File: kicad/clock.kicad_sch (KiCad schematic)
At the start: 182 parts, among them J1 USB4160-03-0230-C, J10 Knob: EM14 enc+SW (top face), J11 Radio-off toggle (rear), J12 NeoPixel ext (5V/DATA/GND, po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, J2 PROG, J3 Speaker DMA58-4 (4R), J6 DM3AT-SF-PEJM5, J7 Sensor board (BME688+TSL2591+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, J9 Wake COB 12V (warm+cool), M1 X40.879, Q1 2N7002, Q2 AO3401A, Q3 2N7002, Q4 AO3401A, Q6 AO3400A, Q7 AO3400A, Q8 2N7002, Q9 AO3401A, SW1 RESET, SW2 BOOT, U1 CH224K, U10 LTC4412ES6, U11 TB6612FNG, U12 TB6612FNG, U13 MCP23017, U14 QRE1113GR, U15 SN74AHCT1G125, U16 USBLC6-2SC6, U2 LT3652EMSE, U3 HY2111-GB, U4 AOSD32334C, U5 TPS61023, U6 TLV62569DBVR, U7 TPS55340PWPR, U8 ESP32-S3-WROOM-1-N16R8, U9 TAS5760MDAPR, Y1 32.768kHz

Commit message: review phase 0+1: fix the three blocking schematic defects
Adds kicad/REVEIW.md (full design review of clock.kicad_sch/.kicad_pcb at
7ec2534) and fixes the three findings that stop the board working:

#1 Q4 (LTC4412 PVDD mux) had drain on PVDD and source on +5V, so its body
   diode dumped the 12 V rail into +5V the moment BOOST12_EN went high --
   past abs-max for U5 (7 V), U6 (6 V), U15 (7 V), the SK6812s and the EM14.
   Now drain->+5V, source->PVDD per the LTC4412 datasheet.

#2 TAS5760M PBTL tied OUTA+||OUTB+ and OUTA-||OUTB-, shorting two anti-phase
   half-bridges (hard PVDD->PGND every switching cycle). TI SLOS772F fig.64/65
   pair A+||A- and B+||B-; bootstraps follow their own leg (C181/C182 swap
   roles, positions unchanged).

#3 LT3652 C_TIMER was 100 nF = 26 min EOC and a 3.3 min precondition window,
   which latches a flat cell off as a bad battery. 1 uF -> 4.4 h / 33 min,
   same 0603 land and an existing BOM line.

Supporting changes:
- pcb_build.py: refuse to run without PCB_BUILD_WIPE_ROUTING=1. It builds with
  CreateEmptyBoard() and would destroy the 1884 routed segments / 555 vias /
  4 filled zones the board has carried since 91c5087.
- sch2.py: _xf() mirrored before rotating, KiCad mirrors after -- silently
  swaps the mirror axes at rot 90/270. Latent until Q4 needed a mirror.
- parts_db.py: fold M1's hand-written "DO NOT MOUNT" assembly note into the
  Notes field, so stamp_bom.py stops wiping it on every run.
- review_check.py: standing assertions for the review findings.

ERC 0. Netlist diff vs the pre-fix schematic is exactly the 6 intended node
moves. PCB routing untouched -- the F8 sync and re-route are still to do.

Co-Authored-By: Claude Opus 5 <noreply@anthropic.com>
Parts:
- C104: value 100nF -> 1uF; MPN CL10B104KB8NNNC -> CL10B105KA8NNNC
- M1: Notes Custom footprint; shafts pass through the board. Long lead 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 -> DO NOT MOUNT. Customer will mount part after PCB reception.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
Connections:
- net +5V: now also Q4.3 (D); no longer Q4.2 (S)
- net PVDD: now also Q4.2 (S); no longer Q4.3 (D)
- net at C181.2, C183.2, L6.1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: now also U9.20 (SPK_OUTB+); no longer U9.26 (SPK_OUTA-)
- net at C182.1: now also U9.25 (BSTRPA-); no longer U9.19 (BSTRPB+)
- net at C180.2, C182.2, L5.1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: now also U9.26 (SPK_OUTA-); no longer U9.20 (SPK_OUTB+)
- net at C181.1: now also U9.19 (BSTRPB+); no longer U9.25 (BSTRPA-)
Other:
- company: Tibo Mauron -> (none)
- title: Wooden Clock - main board -> Wooden Smart Clock — main board
- moved on the sheet: Q4

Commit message: review phase 1b: cheap schematic follow-ons (#11 #12 #15 #17)
#11 J7 pin 6 was NC here but the sensor board drives ALS_INT (TSL2591 INT)
    onto it, so the light sensor could only be polled. Landed on the
    expander's free GPB3.
#12 J7 value string said LIS3DH; the sensor board carries a BNO085.
#15 With VBAT_DIV_EN low, Q3 opens the bottom of the divider and R22 pulls
    the ADC node to V_cell (~4.05 V) -- above the ESP32's VDD+0.3 abs-max, so
    IO1 sits forward-biasing its own upper ESD diode. D14 (same BAT42W/SOD-123
    as D13, no new BOM line) clamps it to ~3.5 V.
#17 Encoder A/B divider 100k/200k -> 10k/20k: same 1:2 ratio and the same
    worst-case 3.5 V at the pin, but 6.7k instead of 66.7k driving a ~40 mm
    run past both stepper drivers and the class-D amp. Costs 2x167 uA.

#13 (R1 dissipating 137 mW in a 100 mW 0603) is deliberately NOT in this
batch: it needs a 1206 land or a high-power 0603 part, i.e. an MPN sourced
and verified, and a _REF override since parts_db keys resistors by value only.

ERC 0. Netlist diff vs 1f3736a is exactly: +ALS_INT (J7.6+U13.4), D14 onto
+3V3/VBAT_SENSE, the two unconnected- pseudo-nets gone, and 5 value changes.
PCB still untouched -- D14 needs placing, and the Phase 2 re-route is next.

Co-Authored-By: Claude Opus 5 <noreply@anthropic.com>
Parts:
- added D14: BAT42W, Diode_SMD:D_SOD-123, symbol Device:D_Schottky
- J7: value Sensor board (BME688+TSL2591+LIS3DH) -> Sensor board (BME688+TSL2591+BNO085)
- R111, R112: value 100k -> 10k; MPN RC0603FR-07100KL -> RC0603FR-0710KL
- R114, R115: value 200k -> 20k; MPN RC0603FR-07200KL -> RC0603FR-0720KL
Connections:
- net +3V3: now also D14.1 (K)
- net VBAT_SENSE: now also D14.2 (A)
- net ALS_INT: now reaches J7.6 (Pin_6)
- net ALS_INT: now also U13.4 (GPB3)
- no-connect marks 20 -> 18

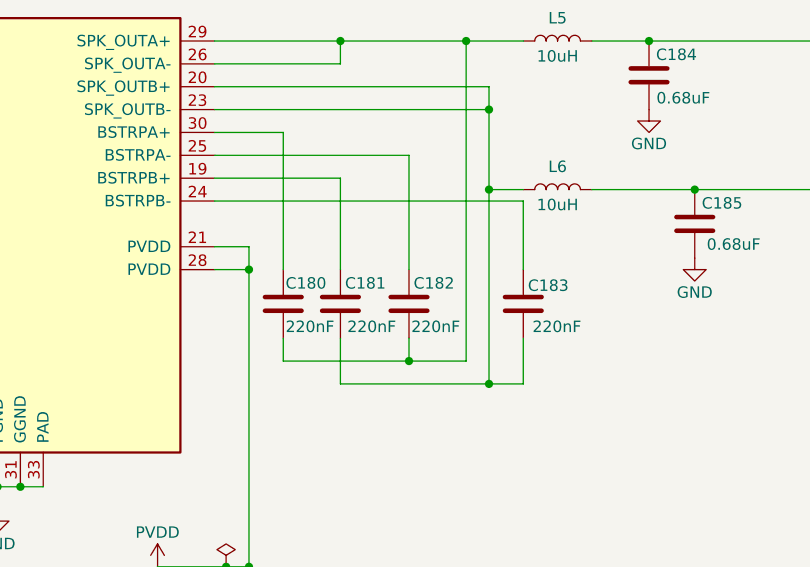
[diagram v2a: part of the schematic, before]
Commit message: review phase 2 prep: swap C181/C182 so the PCB fix for #2 gets cheap
The PBTL re-tie can be satisfied two ways, and they cost very different
amounts of PCB rework:

  X (previous): keep the caps where they are, move the bootstrap PIN
    connections -> U9.25->C182.1 and U9.19->C181.1, two ~6.3 mm routes that
    cross each other and the PVDD/BSTRPB- knot.
  Y (this commit): swap C181/C182 positions so each cap sits on its own leg's
    column. Both caps keep their ORIGINAL U9 pin, which is exactly what the
    existing PCB copper already does, so those two connections need no rework
    at all -- only the two far pads move, as 3.65 mm straight verticals.

Net effect on the PCB: 2 long crossing routes -> 2 short straight ones.

Also measured the U9 fan-out to pick the escape layer: in the 5.7x8.0 mm box
B.Cu carries 47.5 mm over 8 nets, In1 60.3 mm/5, In2 24.7 mm/3, plus 8 vias
and 8 pads -- and F.Cu is completely empty. F.Cu + 2 vias is the way through,
for both the U9 pad swaps and the Q4 +5V hop (where pads 1/2 leave a 0.43 mm
gap and a 0.25 mm track needs 0.45 mm, so B.Cu cannot pass between them).

REVEIW.md now carries the full Phase 2 work order with measured coordinates
and the exact segment numbers to delete.

ERC 0, review_check 7/8 with 0 regressions.

Co-Authored-By: Claude Opus 5 <noreply@anthropic.com>
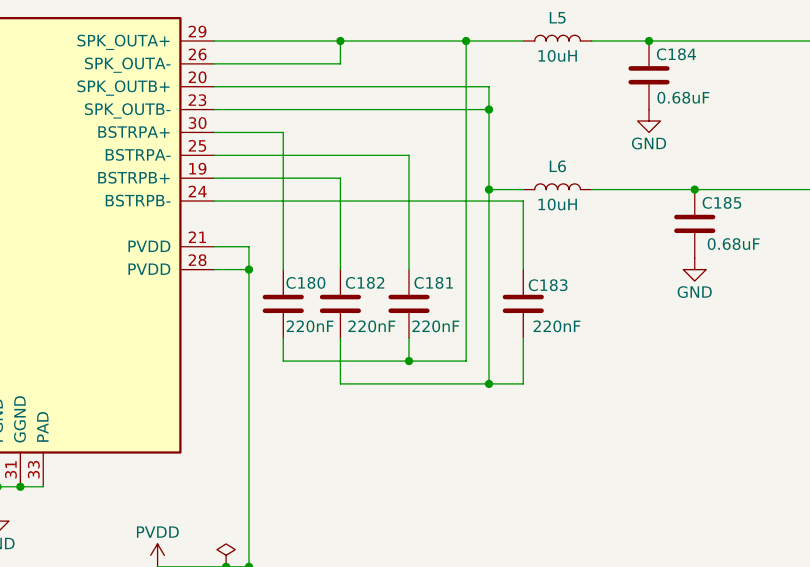
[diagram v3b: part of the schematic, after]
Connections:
- net at C183.2, L6.1, U9.20 (SPK_OUTB+)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: now also C182.2; no longer C181.2
- net at U9.25 (BSTRPA-): now also C181.1; no longer C182.1
- net at C180.2, L5.1, U9.26 (SPK_OUTA-)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: now also C181.2; no longer C182.2
- net at U9.19 (BSTRPB+): now also C182.1; no longer C181.1

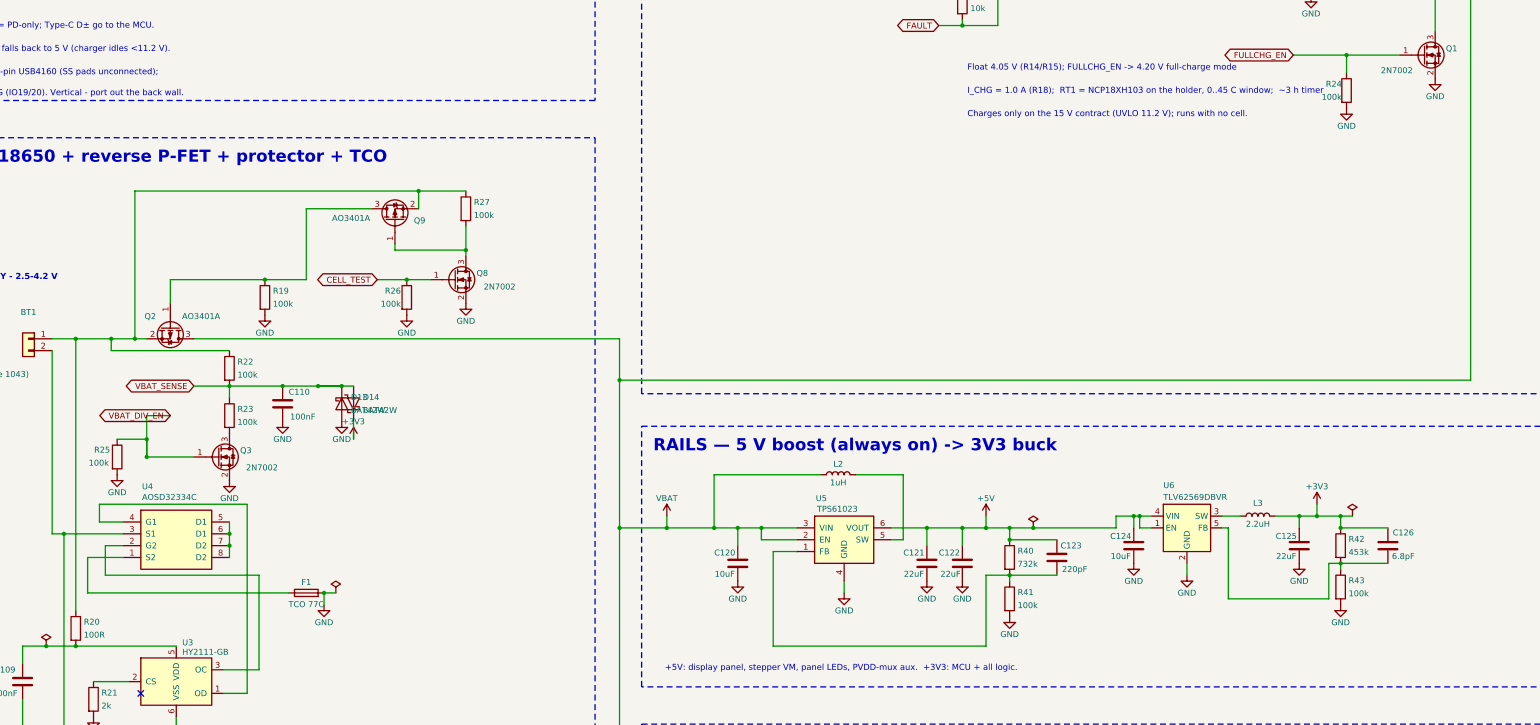
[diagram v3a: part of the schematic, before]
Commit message: review: #10 silkscreen, #13 R1 1206, #20 R20 200R, #21/#16 into FIRMWARE.md
Renames REVEIW.md -> REVIEW.md and restructures it around a status overview
(Fixed / Open / Deferred / Accepted) with a "Fixed in <commit>" column.

#10 Connector kept as-is per decision; disambiguated with silkscreen instead.
    Added "SENSOR" and "KNOB" on B.SilkS -- labelling only J7 would still let
    the pair be swapped. First placement collided with J7's own outline (14
    silk_overlap warnings); moved to (94.5, 13.4) where DRC is clean.
#13 R1 -> 1206 / RC1206FR-071KL (1/4 W). On the 15 V contract it dissipates
    137 mW feeding the CH224K's 3.3 V shunt: 1.4x a 0603 and 1.1x an 0805, so
    1206 is the first standard land with real margin. Needed a _REF override
    since parts_db keys resistors by value only, plus R1206 in sch2.FP and
    _CASE. R1 has 4.6 mm of clear space, so the land swap fits.
#20 R20 100R -> 200R (HYCON's stated max; typ 100R). The protector's VDD sits
    on cell+, so a reversed cell drives VDD ~3.7 V below VSS and this resistor
    is the only limit into the IC's ESD structures: 37 mA -> 18 mA. The added
    overcharge-detection offset is I_VDD (uA) x 100R, well under a mV.
#21 -> FIRMWARE.md R-BOARD-1: set IOCON.MIRROR=1 before enabling any MCP23017
    interrupt (INTA/INTB are tied; push-pull outputs would contend).
#16 -> FIRMWARE.md R-BOARD-2: never assert CELL_TEST unless PD_PG is live.
    Marked deferred in REVIEW.md with the reasoning: it is a self-recovering
    reset loop, not damage.
#14 marked deferred (mostly wall-powered), #22 marked accepted.
#24 recommendation written up: fix the C145/C146 placement during the routing
    pass, keep the ABS07, verify startup on the first article, add a firmware
    oscillator-failure fallback.

Also flags that FIRMWARE.md 6.5 still lists LIS3DH @0x18 while the sensor
board carries a BNO085 -- a different address and a far heavier driver. Left
as a decision, not silently changed.

ERC 0. DRC 0 violations / 0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
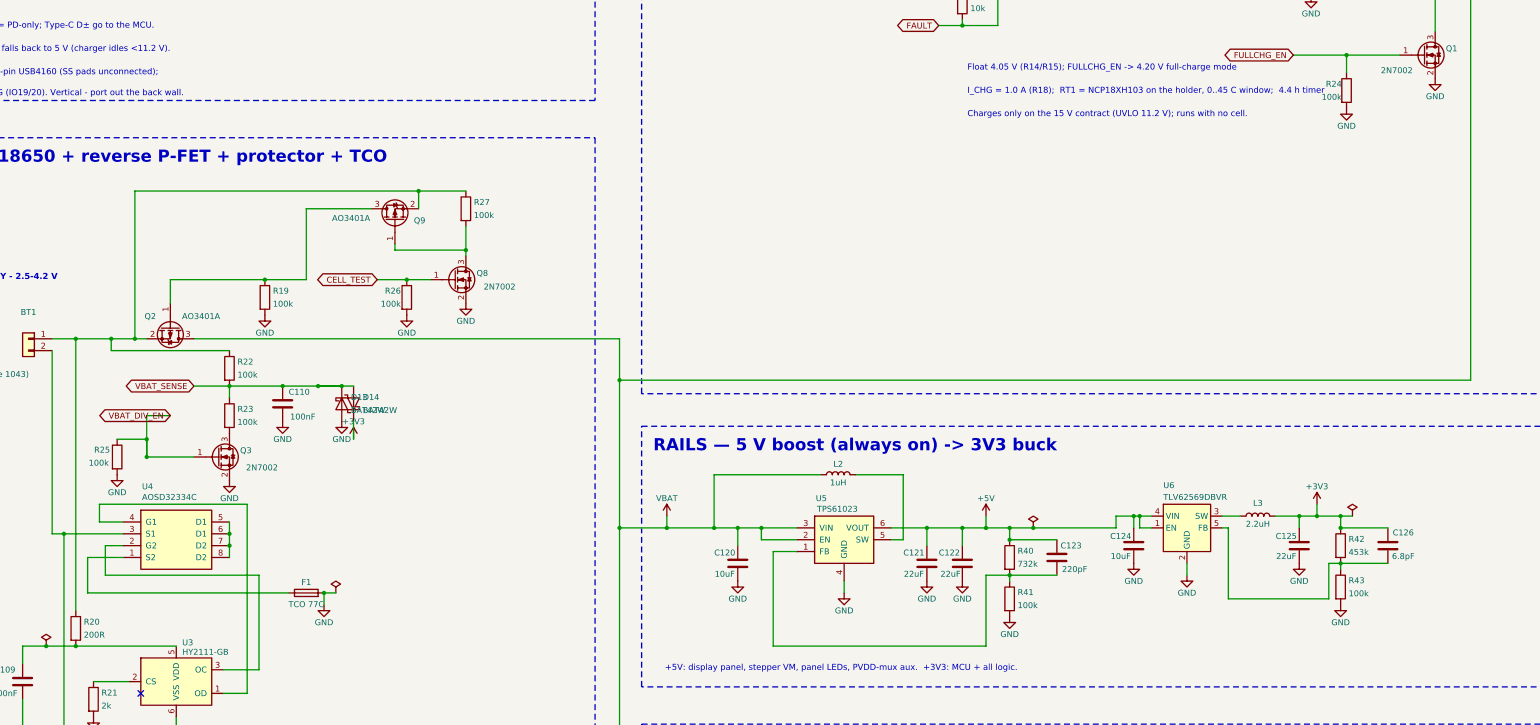
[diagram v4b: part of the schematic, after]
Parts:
- R1: footprint Resistor_SMD:R_0603_1608Metric -> Resistor_SMD:R_1206_3216Metric; MPN RC0603FR-071KL -> RC1206FR-071KL; Notes Substitution OK - same value/tolerance/voltage/dielectric/s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 -> 1206 for the power rating, NOT 0603 -- see REVIEW.md #13; Package 0603 -> 1206
- R20: value 100R -> 200R; MPN RC0603FR-07100RL -> RC0603FR-07200RL
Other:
- note added: "I_CHG = 1.0 A (R18); RT1 = NCP18XH103 on the holder, 0..45 C window; 4.4 h timer"
- note removed: "I_CHG = 1.0 A (R18); RT1 = NCP18XH103 on the holder, 0..45 C window; ~3 h timer"
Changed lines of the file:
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@@
 		)
 	)
-	(text "I_CHG = 1.0 A (R18);  RT1 = NCP18XH103 on the holder, 0..45 C window;  ~3 h timer"
+	(text "I_CHG = 1.0 A (R18);  RT1 = NCP18XH103 on the holder, 0..45 C window;  4.4 h timer"
 		(exclude_from_sim no)
 		(at 250 150 0)
@@
 			)
 		)
-		(property "Footprint" "Resistor_SMD:R_0603_1608Metric"
+		(property "Footprint" "Resistor_SMD:R_1206_3216Metric"
 			(at 114.3 63.5 0)
 			(hide yes)
@@
 			)
 		)
-		(property "Package" "0603"
+		(property "Package" "1206"
 			(at 114.3 63.5 0)
 			(hide yes)
@@
 			)
 		)
-		(property "MPN" "RC0603FR-071KL"
+		(property "MPN" "RC1206FR-071KL"
 			(at 114.3 63.5 0)
 			(hide yes)
@@
 			)
 		)
-		(property "Description" "RES 1K OHM 1% 1/10W 0603"
+		(property "Description" "RES 1K OHM 1% 1/4W 1206"
 			(at 114.3 63.5 0)
 			(hide yes)
@@
 			)
 		)
-		(property "Notes" "Substitution OK - same value/tolerance/voltage/dielectric/size"
+		(property "Notes" "1206 for the power rating, NOT 0603 -- see REVIEW.md #13"
 			(at 114.3 63.5 0)
 			(hide yes)
@@
 			)
 		)
-		(property "Value" "100R"
+		(property "Value" "200R"
 			(at 60.136 266.83 0)
 			(show_name no)
@@
 			)
 		)
-		(property "MPN" "RC0603FR-07100RL"
+		(property "MPN" "RC0603FR-07200RL"
 			(at 58.42 265.43 0)
 			(hide yes)
@@
 			)
 		)
-		(property "Description" "RES 100 OHM 1% 1/10W 0603"
+		(property "Description" "RES 200 OHM 1% 1/10W 0603"
 			(at 58.42 265.43 0)
 			(hide yes)

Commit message: review: #19 PVDD bulk ripple rating, #16 comment correction
#19 C172 was a plain low-ESR electrolytic (Rubycon 25TZV100M6.3X8) rated
    300 mA @100 kHz. A class-D BTL draws i_supply = P/PVDD x (1 - cos 2wt),
    so the bulk sees (P/PVDD)/sqrt(2) rms at twice the audio frequency:

        8 W (firmware limit) / 11.5 V -> 0.49 A rms
        11 W (clip)          / 11.5 V -> 0.68 A rms

    i.e. under-rated ~1.6x at the limit the firmware already enforces. Swapped
    to a hybrid polymer in the SAME D6.3 land -- Panasonic EEH-ZA1E101P,
    100 uF/25 V, ~1.3 A ripple, ~40 mOhm ESR -- so this stays a pure BOM change
    with no PCB impact. 7.7 mm also fits the CP_Elec_6.3x7.7 land better than
    the old 8.0 mm can. A substitution rule is recorded in parts_db (any D6.3,
    >=600 mA @100 kHz, >=25 V; value may drop to 68 uF if that buys the
    rating) so any swap is checkable.

#16 The CELL_TEST comment in b_charger.py claimed "on battery Q2's body diode
    keeps the system alive but drops ~0.4 V". That is wrong, and it is exactly
    the sentence that would make someone think this is safe on battery: Q2 is
    a P-FET with S=holder+ and D=VBAT, so its body diode conducts VBAT->holder+
    only and discharge current has to flow the other way. With Q2 off on
    battery the system loses power outright. The comment now states the real
    behaviour (self-recovering reset loop, not damage) and points at
    FIRMWARE.md R-BOARD-2.

Also bumps the drawing date to 2026-08-04; it still read 2026-07-14 despite
the schematic having changed materially.

ERC 0. review_check 8/12, 0 regressions (the 4 TODOs are all PCB items).

Co-Authored-By: Claude Opus 5 <noreply@anthropic.com>
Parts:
- C172: MPN 25TZV100M6.3X8 -> EEH-ZA1E101P; Manufacturer Rubycon -> Panasonic; Notes PVDD bulk. Was 220uF: no tier-1 220uF >=16V exists in a D6.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 -> PVDD bulk. **Hybrid polymer, NOT a plain electrolytic** -- 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; Package SMD radial can D6.3xL8.0mm -> SMD radial can D6.3xL7.7mm
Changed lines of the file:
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@@
 	(title_block
 		(title "Wooden Smart Clock — main board")
-		(date "2026-07-14")
+		(date "2026-08-04")
 		(rev "A")
 	)
@@
 			)
 		)
-		(property "Package" "SMD radial can D6.3xL8.0mm"
+		(property "Package" "SMD radial can D6.3xL7.7mm"
 			(at 751.84 293.37 0)
 			(hide yes)
@@
 			)
 		)
-		(property "MPN" "25TZV100M6.3X8"
+		(property "MPN" "EEH-ZA1E101P"
 			(at 751.84 293.37 0)
 			(hide yes)
@@
 			)
 		)
-		(property "Manufacturer" "Rubycon"
+		(property "Manufacturer" "Panasonic"
 			(at 751.84 293.37 0)
 			(hide yes)
@@
 			)
 		)
-		(property "Description" "CAP ALUM 100UF 25V 20% LOW-ESR SMD"
+		(property "Description" "CAP ALUM POLY HYBRID 100UF 25V SMD"
 			(at 751.84 293.37 0)
 			(hide yes)
@@
 			)
 		)
-		(property "Notes" "PVDD bulk. Was 220uF: no tier-1 220uF >=16V exists in a D6.3 can (Panasonic/Nichicon are D8), so the value dropped to 100uF/25V (2026-07-27). TZV = low-ESR, 300 mA @100 kHz, 2000 h/105 C. DigiKey alt: Nichicon UWT1E101MCL1GS (D6.3x7.7, 137 mA ripple)"
+		(property "Notes" "PVDD bulk. **Hybrid polymer, NOT a plain electrolytic** -- the ripple rating is the spec that matters here, not the value. A class-D BTL draws i_supply = P/PVDD x (1-cos 2wt), so the bulk sees (P/PVDD)/sqrt(2) rms at twice the audio frequency: 0.49 A at the 8 W firmware limit, 0.68 A at clip. The previous part (Rubycon 25TZV100M6.3X8, 300 mA @100 kHz) was under-rated ~1.6x; the ZA hybrid is ~1.3 A with ~40 mOhm ESR, and 7.7 mm actually fits the CP_Elec_6.3x7.7 land better than the old 8.0 mm can. SUBSTITUTION RULE: any D6.3 part with >=600 mA @100 kHz ripple and >=25 V. Value may drop to 68 uF if that buys the rating. VERIFY DigiKey stock before ordering (REVIEW.md #19)"
 			(at 751.84 293.37 0)
 			(hide yes)
